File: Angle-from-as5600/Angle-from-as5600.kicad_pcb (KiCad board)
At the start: 2 copper layers, 19 x 40.6 mm, 14 parts, among them J1 Conn_01x03_Pin, J3 Conn_01x05_Socket, U1 AS5600

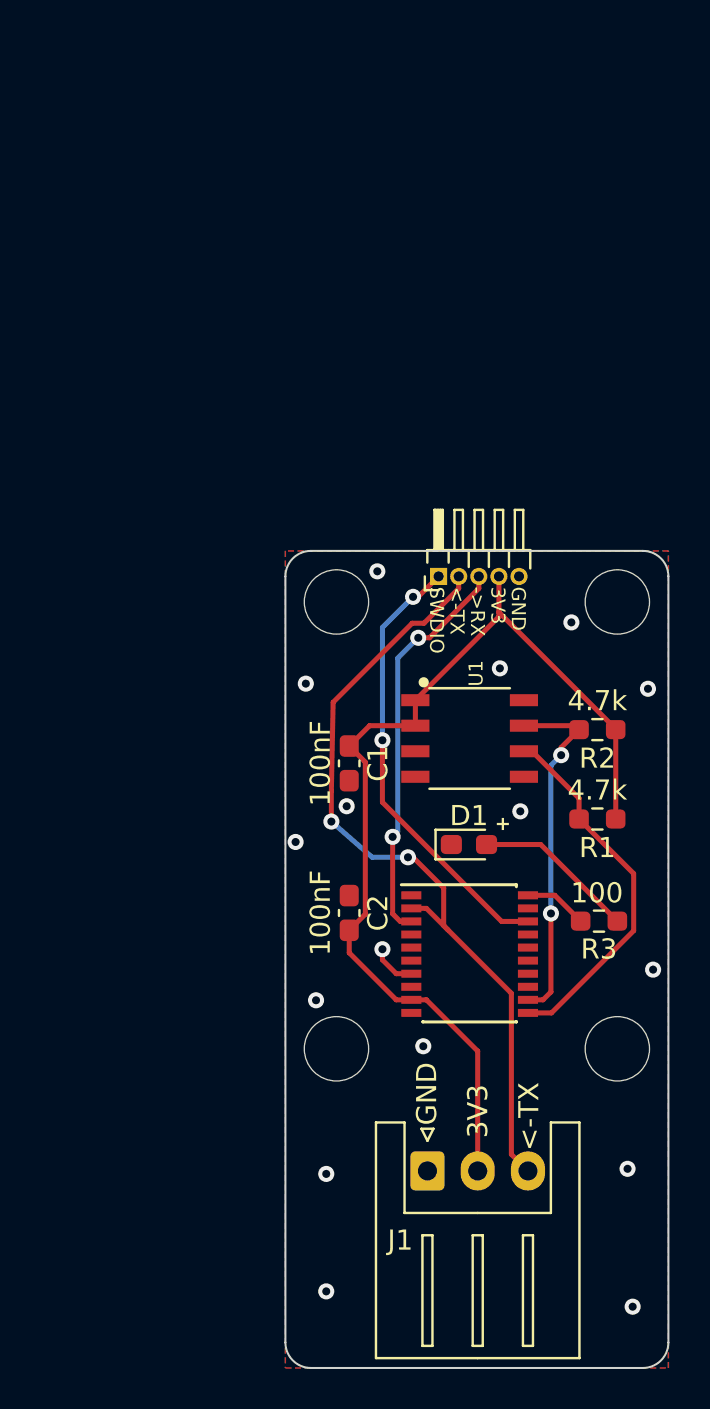
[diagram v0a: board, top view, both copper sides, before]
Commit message: fix kicad files
fix pin pitch
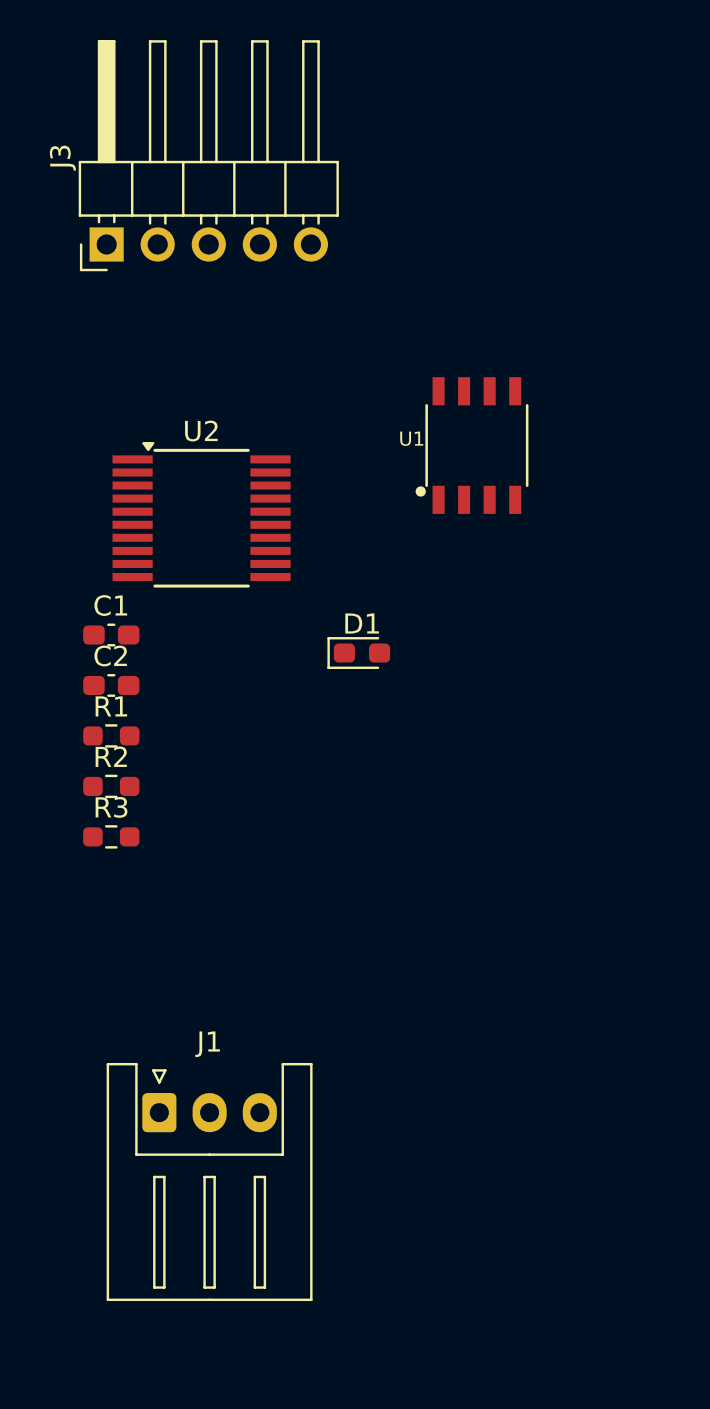
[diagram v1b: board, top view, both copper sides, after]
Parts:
- removed REF** (x4): MountingHole_3.2mm_M3, MountingHole:MountingHole_3.2mm_M3
- J3: footprint Connector_PinHeader_1.00mm:PinHeader_1x05_P1.00mm_Horizontal -> Connector_PinHeader_2.54mm:PinHeader_1x05_P2.54mm_Horizontal
- U2: footprint Package_SO:SSOP-20_4.4x6.5mm_P0.65mm -> Package_SO:SSOP-20_4.4x6.5mm_P0.65mm_bigpad
- moved U2 25.5 mm to (152.0, 84.7)
- moved R3 24.6 mm to (147.6, 100.6)
- moved R1 24.5 mm to (147.6, 95.6), turned to 0 degrees
- moved R2 24.3 mm to (147.6, 98.1), turned to 0 degrees
- moved J3 23.3 mm to (147.3, 71.1)
- moved C2 16.4 mm to (147.6, 93.1), turned to 0 degrees
- moved U1 14.6 mm to (165.7, 81.1), turned to 0 degrees
- moved J1 13.6 mm to (149.9, 114.3)
- moved C1 13.4 mm to (147.6, 90.5), turned to 0 degrees
- moved D1 10.9 mm to (160.0, 91.4)
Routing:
- net +3V3: track 50.9 -> 0.00 mm
- net chTX: track 40.1 -> 0.00 mm, vias 2 -> 0
- net SWDIO: track 22.5 -> 0.00 mm, vias 2 -> 0
- net chRX: track 20.0 -> 0.00 mm, vias 2 -> 0
- net SDA: track 18.4 -> 0.00 mm
- net SCL: track 17.8 -> 0.00 mm, vias 2 -> 0
- net Net-(D1-A): track 8.08 -> 0.00 mm
- net Net-(U2-PD3): track 3.15 -> 0.00 mm
- net GND: track 2.25 -> 0.00 mm, vias 16 -> 0
- removed copper zone on B.Cu, net GND
- removed copper zone on F.Cu, net GND
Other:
- board outline removed
- board text removed: "+"
- board text removed: "->RX"
- board text removed: "3V3"
- board text removed: "<-TX"
- board text removed: "GND"
- board text removed: "SWDIO"
